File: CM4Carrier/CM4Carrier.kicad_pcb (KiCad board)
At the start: 2 copper layers, 125 x 84 mm, 137 parts, among them J1 Micro_SD_Card, J2 Conn_01x04_Female, J3 USB_A, J4 USB_C_Receptacle_USB2.0, J5 1-84952-5, J6 AudioJack3_Dual_Ground_Switch, SW1 SW_Push, SW10 SW_Push, SW11 SW_Push, SW2 SW_Push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

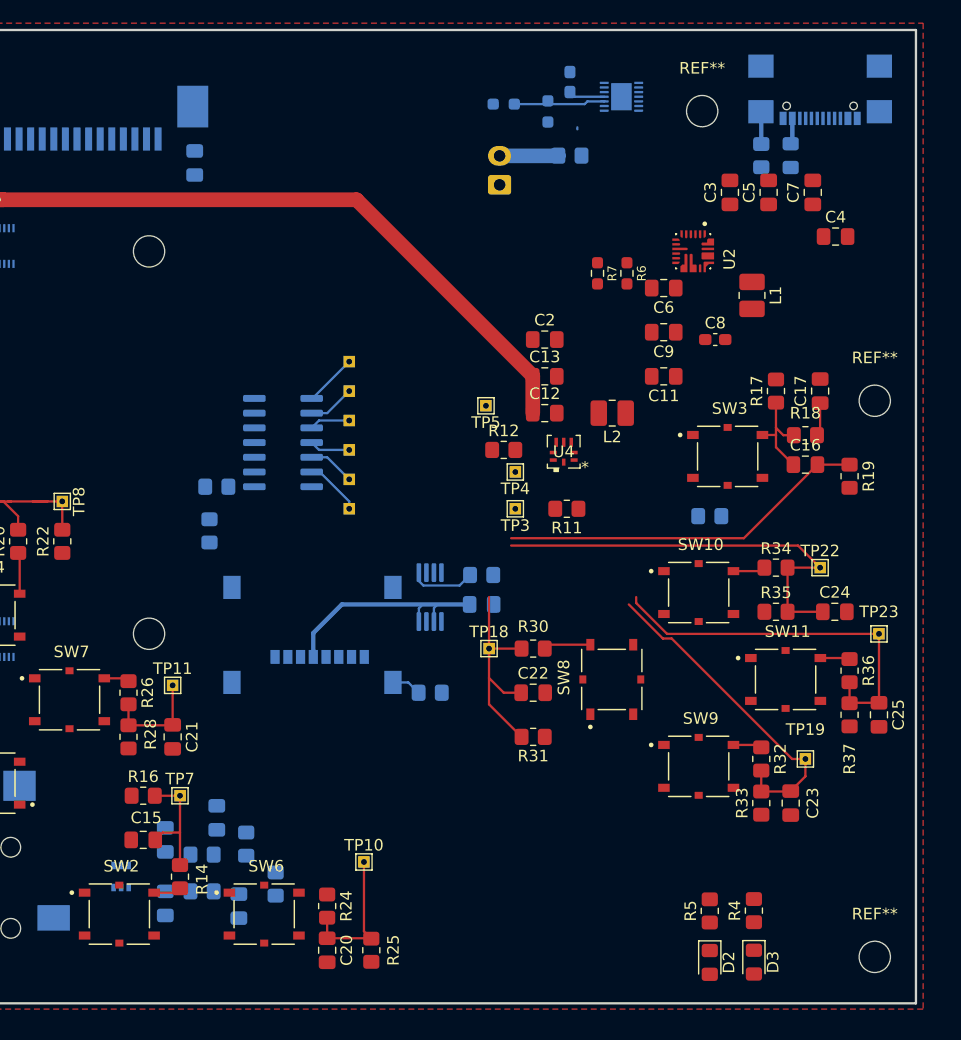
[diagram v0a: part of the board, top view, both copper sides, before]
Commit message: add buttons
need to adjust 3d model for buttons and add them to pcb... forgot about these.
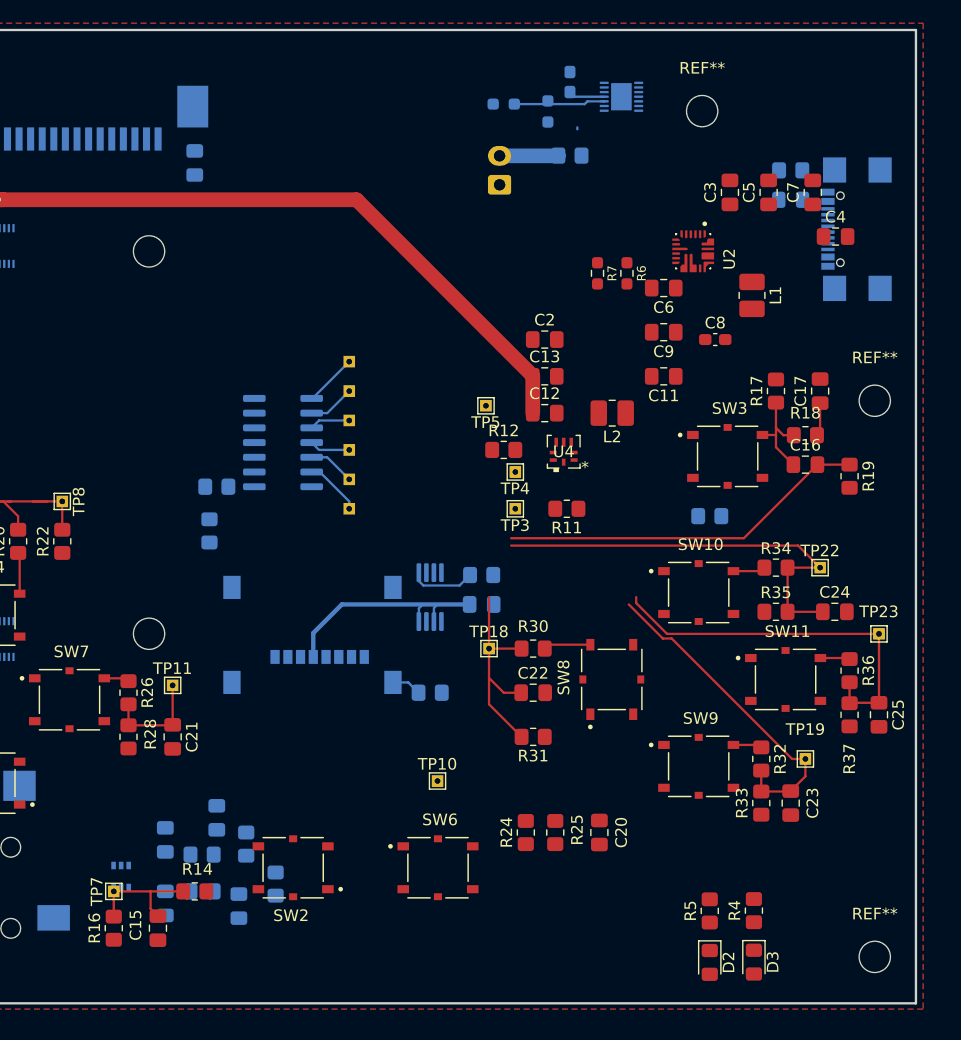
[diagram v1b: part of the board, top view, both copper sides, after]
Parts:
- moved C20 25.6 mm to (176.5, 125.7)
- moved R25 18.8 mm to (172.7, 125.7)
- moved R24 18.3 mm to (170.2, 125.7), turned to 90 degrees
- moved SW2 15.5 mm to (150.1, 128.8), turned to 180 degrees
- moved SW6 15.5 mm to (162.6, 128.8)
- moved R16 11.7 mm to (134.6, 134.0), turned to 90 degrees
- moved J4 10.8 mm to (197.3, 73.7), turned to -90 degrees
- moved TP7 10.0 mm to (134.6, 130.8), turned to 90 degrees
- moved TP10 9.44 mm to (162.6, 121.3)
- moved C15 7.73 mm to (138.4, 134.0), turned to -90 degrees
- moved F2 3.81 mm to (193.0, 71.1), turned to 180 degrees
- moved R38 2.84 mm to (193.0, 68.6), turned to 180 degrees
- moved R14 1.80 mm to (141.6, 130.8), turned to 180 degrees
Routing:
- net /bi1: track 12.5 -> 0.00 mm
- net Net-(J4-PadS1): track 2.80 -> 0.00 mm
- net Net-(J4-PadA4/B9): track 2.25 -> 0.00 mm
- net Net-(R14-Pad1): track 2.39 -> 0.54 mm

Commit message: aa
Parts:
- added C31: 100nF, Capacitor_SMD:C_0805_2012Metric_Pad1.18x1.45mm_HandSolder, F.Cu at (226.1, 88.9)
- added C32: 100nF, Capacitor_SMD:C_0805_2012Metric_Pad1.18x1.45mm_HandSolder, F.Cu at (221.2, 88.9)
- added C33: 100nF, Capacitor_SMD:C_0805_2012Metric_Pad1.18x1.45mm_HandSolder, B.Cu at (135.4, 41.3)
- added C34: 100nF, Capacitor_SMD:C_0805_2012Metric_Pad1.18x1.45mm_HandSolder, B.Cu at (140.2, 41.3)
- added R43: 1k, Resistor_SMD:R_0805_2012Metric_Pad1.20x1.40mm_HandSolder, F.Cu at (249.0, 74.6)
- added R44: 1k, Resistor_SMD:R_0805_2012Metric_Pad1.20x1.40mm_HandSolder, F.Cu at (230.8, 88.9)
- added R45: 1k, Resistor_SMD:R_0805_2012Metric_Pad1.20x1.40mm_HandSolder, B.Cu at (135.5, 44.3)
- added R46: 1k, Resistor_SMD:R_0805_2012Metric_Pad1.20x1.40mm_HandSolder, B.Cu at (130.6, 41.2)
- added R47: 10k, Resistor_SMD:R_0805_2012Metric_Pad1.20x1.40mm_HandSolder, F.Cu at (239.4, 80.5)
- added R48: 10k, Resistor_SMD:R_0805_2012Metric_Pad1.20x1.40mm_HandSolder, F.Cu at (244.1, 80.5)
- added R49: 10k, Resistor_SMD:R_0805_2012Metric_Pad1.20x1.40mm_HandSolder, B.Cu at (140.2, 44.3)
- added R50: 10k, Resistor_SMD:R_0805_2012Metric_Pad1.20x1.40mm_HandSolder, B.Cu at (122.1, 34.1)
- added SW12: SW_Push, CM4IO:SW_PTS526_SMG15_SMTR2_LFS, F.Cu at (223.6, 83.8)
- added SW13: SW_Push, CM4IO:SW_PTS526_SMG15_SMTR2_LFS, F.Cu at (223.6, 76.7)
- added SW14: SW_Push, CM4IO:SW_PTS526_SMG15_SMTR2_LFS, B.Cu at (123.3, 121.0)
- added SW15: SW_Push, CM4IO:SW_PTS526_SMG15_SMTR2_LFS, B.Cu at (159.3, 121.0)
- added TP25: A, TestPoint:TestPoint_THTPad_1.0x1.0mm_Drill0.5mm, F.Cu at (248.0, 80.7)
- added TP26: A, TestPoint:TestPoint_THTPad_1.0x1.0mm_Drill0.5mm, F.Cu at (243.3, 83.5)
- added TP27: A, TestPoint:TestPoint_THTPad_1.0x1.0mm_Drill0.5mm, F.Cu at (248.0, 77.6)
- added TP27: A, TestPoint:TestPoint_THTPad_1.0x1.0mm_Drill0.5mm, B.Cu at (122.9, 37.1)
- added TP28: A, TestPoint:TestPoint_THTPad_1.0x1.0mm_Drill0.5mm, F.Cu at (239.5, 86.5)
- added TP28: A, TestPoint:TestPoint_THTPad_1.0x1.0mm_Drill0.5mm, B.Cu at (131.4, 44.2)
- moved SW10 11.5 mm to (173.6, 105.0)
- moved SW11 11.5 mm to (181.1, 112.5)
- moved SW9 11.5 mm to (173.6, 120.0)
- moved SW8 11.5 mm to (166.1, 112.5)
- moved R34 10.8 mm to (181.0, 102.9)
- moved R35 10.8 mm to (181.0, 106.7)
- moved R36 10.8 mm to (187.3, 111.8)
- moved R37 10.8 mm to (187.3, 115.6)
- moved TP19 10.8 mm to (183.5, 119.4)
- moved TP22 10.8 mm to (184.8, 102.9)
- moved C22 10.8 mm to (160.0, 113.7)
- moved C23 10.8 mm to (182.2, 123.2)
- moved C24 10.8 mm to (186.1, 106.7)
- moved C25 10.8 mm to (189.9, 115.6)
- moved R30 10.8 mm to (160.0, 109.9)
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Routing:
- net Net-(R34-Pad1): track 2.79 -> 3.92 mm
- net Net-(R32-Pad1): track 2.49 -> 3.49 mm
- net Net-(R36-Pad1): track 2.56 -> 3.39 mm
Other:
- outline, holes or cut-outs redrawn

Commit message: aa
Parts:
- moved R40 45.2 mm to (114.3, 146.7), turned to -90 degrees
- moved R39 43.5 mm to (116.8, 150.1), turned to -90 degrees
- moved C27 41.9 mm to (119.4, 152.4), turned to -90 degrees
- moved C28 38.0 mm to (117.5, 144.8), turned to 90 degrees
- moved R41 36.1 mm to (120.7, 149.2), turned to 180 degrees
- moved R42 32.9 mm to (120.7, 146.0), turned to 180 degrees
- moved C29 32.8 mm to (123.8, 150.5), turned to -90 degrees
- moved C30 26.3 mm to (123.8, 145.0), turned to 90 degrees
- moved D4 22.9 mm to (127.6, 147.3), turned to 90 degrees
- moved R16 21.3 mm to (144.1, 114.9), turned to 0 degrees
- moved TP7 16.5 mm to (148.0, 116.8), turned to 0 degrees
- moved C15 16.3 mm to (144.1, 118.7), turned to 180 degrees
- moved R14 10.6 mm to (147.3, 121.9), turned to 90 degrees
- moved TP20 6.35 mm to (99.7, 134.6)
- moved TP21 6.35 mm to (92.7, 134.6)
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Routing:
- net /IO B/DSI0_L0_DP1: track 0.00 -> 48.7 mm, vias 0 -> 2
- net /IO B/DSI0_L0_DN1: track 0.00 -> 48.0 mm, vias 0 -> 2
- net /IO B/DSI0_CP: track 0.00 -> 45.8 mm, vias 0 -> 2
- net /IO B/DSI0_CN: track 0.00 -> 45.7 mm, vias 0 -> 2
- net /IO B/DSI0_L1_DP1: track 0.00 -> 45.1 mm, vias 0 -> 2
- net /IO B/DSI0_L1_DN1: track 0.00 -> 45.1 mm, vias 0 -> 2
- net /3v3: track 0.00 -> 34.0 mm
- net /Battery/BATT__: track 0.00 -> 29.4 mm
- net /bi2: track 29.5 -> 15.9 mm
- net /bi0: track 10.6 -> 0.00 mm
- net Net-(J2-Pad2): track 11.7 -> 4.89 mm
- net Net-(BT1-Pad2): track 5.25 -> 11.7 mm, vias 0 -> 2
- net GND: track 0.00 -> 4.46 mm, vias 0 -> 2
- net /_5v: track 109.6 -> 113.9 mm
- net /IO B/D+: track 45.1 -> 46.1 mm
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- added copper zone on B.Cu, net GND

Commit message: update
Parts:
- moved U6 41.5 mm to (83.2, 101.0), turned to 90 degrees
- moved J2 27.1 mm to (84.5, 117.7), turned to -90 degrees
- moved TP20 22.2 mm to (81.9, 121.3), turned to 90 degrees
- moved R41 15.3 mm to (121.9, 134.0)
- moved R42 15.3 mm to (121.9, 130.8)
- moved R39 15.3 mm to (118.1, 134.9)
- moved C28 15.3 mm to (118.7, 129.5)
- moved C27 15.3 mm to (120.6, 137.2)
- moved C30 15.3 mm to (125.1, 129.8)
- moved D4 15.3 mm to (128.9, 132.1)
- moved R40 15.3 mm to (115.6, 131.4)
- moved C29 15.3 mm to (125.1, 135.3)
- moved TP21 12.5 mm to (81.9, 128.3), turned to 90 degrees
- moved J6 3.18 mm to (137.8, 131.4)
- moved TP18 3.17 mm to (156.2, 104.8)
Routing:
- net /3v3: track 34.0 -> 92.8 mm, vias 0 -> 1
- net /IO/SD_DAT0: track 0.00 -> 55.4 mm, vias 0 -> 2
- net /IO/SD_DAT1: track 0.00 -> 54.8 mm, vias 0 -> 2
- net /IO/SD_CLK: track 0.00 -> 54.4 mm, vias 0 -> 2
- net /IO/SD_DAT2: track 0.00 -> 51.2 mm, vias 0 -> 2
- net Net-(J2-Pad2): track 4.89 -> 17.8 mm, vias 1 -> 0
- net Net-(J2-Pad4): track 17.6 -> 29.3 mm
- net /IO/SD_DAT3: track 0.00 -> 4.82 mm, vias 0 -> 2
- net /IO B/DSI0_L1_DP1: track 45.1 -> 45.9 mm
- net /bi6: track 20.0 -> 20.6 mm
- net /IO B/DSI0_CN: track 45.7 -> 46.2 mm
- net Net-(R14-Pad1): track 0.54 -> 0.00 mm
- net /IO/SD_PWR: track 19.5 -> 19.8 mm, vias 2 -> 0
- net GND: vias 2 -> 10
- added copper zone on In1.Cu, net GND
- added copper zone on In2.Cu, net GND
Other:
- outline, holes or cut-outs redrawn
- copper layers 2 -> 4

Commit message: nearly done
i do not want to do the fiddly ones
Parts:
- moved TP7 9.39 mm to (143.3, 108.7)
- moved TP18 8.60 mm to (154.9, 113.3)
- moved R27 6.48 mm to (143.3, 89.4)
- moved R29 6.48 mm to (142.6, 93.2)
- moved R16 2.16 mm to (146.3, 114.9)
- moved C15 2.16 mm to (146.3, 118.7)
- moved C30 0.23 mm to (125.1, 129.5)
- moved R42 0.23 mm to (121.9, 130.6)
- moved C28 0.23 mm to (118.7, 129.3)
- moved R40 0.23 mm to (115.6, 131.2)
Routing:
- net /Battery/ALRT: track 0.00 -> 86.4 mm, vias 0 -> 2
- net /bi1: track 0.00 -> 85.9 mm, vias 0 -> 1
- net /IO/I2C_SDA: track 0.00 -> 84.2 mm, vias 0 -> 2
- net /IO/AUX_L: track 0.00 -> 83.1 mm, vias 0 -> 2
- net /IO/AUX_R: track 0.00 -> 81.2 mm, vias 0 -> 2
- net /IO/I2C_SCLK: track 0.00 -> 80.9 mm, vias 0 -> 2
- net /bi8: track 28.4 -> 103.4 mm, vias 0 -> 2
- net /bi9: track 32.9 -> 103.7 mm, vias 0 -> 3
- net /bi0: track 0.00 -> 60.8 mm, vias 0 -> 1
- net /IO/SPI0_CE0_N: track 0.00 -> 60.2 mm, vias 0 -> 2
- net /bi7: track 37.1 -> 97.1 mm, vias 0 -> 3
- net /IO/SD_PWR_ON: track 5.68 -> 60.8 mm, vias 0 -> 4
- net /IO/SD_DAT3: track 4.82 -> 59.7 mm
- net /IO/SD_CMD: track 0.00 -> 54.0 mm, vias 0 -> 2
- net /bi5: track 9.04 -> 62.7 mm, vias 0 -> 1
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- added copper zone on In1.Cu, net /3v3
- removed copper zone on In1.Cu, net GND

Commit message: aaaa
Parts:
- C2: footprint Capacitor_SMD:C_0805_2012Metric_Pad1.18x1.45mm_HandSolder -> Capacitor_SMD:C_0603_1608Metric_Pad1.08x0.95mm_HandSolder
- moved R43 255.8 mm to (20.0, 188.7), turned to 90 degrees
- moved TP27 251.3 mm to (23.1, 189.6), turned to 90 degrees
- moved TP25 247.2 mm to (26.2, 189.6), turned to 90 degrees
- moved R48 245.6 mm to (26.0, 193.5), turned to 90 degrees
- moved SW13 243.9 mm to (22.1, 214.0), turned to 90 degrees
- moved R47 243.7 mm to (26.0, 198.3), turned to 90 degrees
- moved TP26 241.2 mm to (29.0, 194.4), turned to 90 degrees
- moved TP28 235.7 mm to (32.0, 198.2), turned to 90 degrees
- moved SW12 233.9 mm to (29.3, 214.0), turned to 90 degrees
- moved R44 229.2 mm to (34.3, 206.8), turned to 90 degrees
- moved C31 227.6 mm to (34.4, 211.6), turned to 90 degrees
- moved C32 226.2 mm to (34.4, 216.4), turned to 90 degrees
- moved R50 92.0 mm to (149.4, 121.9), turned to 90 degrees
- moved C33 83.4 mm to (110.7, 120.9), turned to -90 degrees
- moved C34 81.5 mm to (151.9, 121.9), turned to -90 degrees
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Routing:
- net GND: track 22.6 -> 81.0 mm, vias 20 -> 29
- net /IO/SD_DAT2: track 12.8 -> 68.2 mm
- net Net-(C17-Pad1): track 2.88 -> 57.6 mm, vias 0 -> 2
- net /Battery/BATT__: track 29.4 -> 61.3 mm, vias 0 -> 4
- net /Buttons/GLOBAL-EN: track 2.96 -> 28.5 mm, vias 0 -> 2
- net /BATT_S: track 0.00 -> 24.3 mm, vias 0 -> 1
- net /Battery/CHRG-D-: track 0.00 -> 23.9 mm, vias 0 -> 3
- net /Battery/CHRG-D+: track 0.00 -> 23.4 mm, vias 0 -> 2
- net Net-(C4-Pad1): track 0.00 -> 17.4 mm, vias 0 -> 4
- net /Battery/CHRG-CC1: track 0.00 -> 17.3 mm, vias 0 -> 1
- net /Battery/CHRG-CC2: track 0.00 -> 16.3 mm, vias 0 -> 1
- net /Buttons/SHOULDERL2: track 0.00 -> 15.7 mm
- net Net-(C4-Pad2): track 0.00 -> 12.9 mm, vias 0 -> 4
- net Net-(C8-Pad1): track 0.00 -> 10.2 mm
- net Net-(C2-Pad1): track 0.00 -> 9.78 mm
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- added copper zone on F.Cu, net /BATT_S
- added copper zone on B.Cu, net Net-(C4-Pad2)

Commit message: routing
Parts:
- removed the REF** at (97.3, 63.5)
- removed the REF** at (82.4, 136.5)
- removed the REF** at (82.4, 88.5)
- removed TP20: U/D, TestPoint:TestPoint_THTPad_1.0x1.0mm_Drill0.5mm
- removed TP21: L/R, TestPoint:TestPoint_THTPad_1.0x1.0mm_Drill0.5mm
- C14, R13, R15: moved to B.Cu
- J2, J3, TP27, U6: moved to F.Cu
- moved R1 99.6 mm to (172.5, 29.8), turned to 180 degrees
- moved D1 97.0 mm to (172.5, 32.8), turned to 180 degrees
- moved J3 93.9 mm to (174.9, 131.7)
- moved TP2 92.3 mm to (168.6, 32.8), turned to 180 degrees
- moved F1 89.4 mm to (169.5, 126.4), turned to 90 degrees
- moved R47 88.6 mm to (50.6, 113.2)
- moved R48 88.6 mm to (50.6, 108.4)
- moved SW12 88.6 mm to (53.9, 128.9)
- moved SW13 88.6 mm to (46.7, 128.9)
- moved C31 88.6 mm to (58.9, 126.5)
- moved R43 88.6 mm to (44.6, 103.5)
- moved TP25 88.6 mm to (50.7, 104.5)
- moved TP26 88.6 mm to (53.6, 109.3)
- moved TP27 88.6 mm to (47.7, 104.5)
- moved C32 88.6 mm to (58.9, 131.3)
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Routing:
- net /_5v: track 113.9 -> 40.3 mm, vias 6 -> 3
- net /IO/SPI0_CE0_N: track 60.2 -> 0.00 mm, vias 2 -> 0
- net /Battery/ALRT: track 86.4 -> 36.9 mm, vias 2 -> 1
- net /3v3: track 74.0 -> 24.6 mm, vias 21 -> 17
- net Net-(C16-Pad2): track 61.5 -> 12.8 mm
- net /IO B/D+: track 46.1 -> 0.00 mm
- net /IO B/D-: track 45.4 -> 0.00 mm
- net /Buttons/GLOBAL-EN: track 28.5 -> 73.6 mm
- net /IO/SPI0_MOSI: track 44.9 -> 0.00 mm, vias 2 -> 0
- net /IO/I2C_SDA: track 84.2 -> 42.0 mm, vias 2 -> 1
- net /IO/SPI0_MISO: track 42.0 -> 0.00 mm, vias 2 -> 0
- net /IO/SPIO_SCLK: track 41.7 -> 0.00 mm, vias 2 -> 0
- net /IO/I2C_SCLK: track 80.9 -> 41.4 mm, vias 2 -> 1
- net Net-(C17-Pad1): track 57.6 -> 19.9 mm, vias 2 -> 1
- net /bi3: track 64.2 -> 98.7 mm, vias 2 -> 1
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- added copper zone on B.Cu, net /3v3
- added copper zone on B.Cu, net /_5v
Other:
- board size 125 x 84 mm -> 95.9 x 84 mm
- board text removed: "Hack the planet!"
